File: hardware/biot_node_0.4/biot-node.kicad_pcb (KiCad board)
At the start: 2 copper layers, 13 parts, among them P1 ATSAMR21B, P2 ATSAMR21B-TEST-POINTs, P3 ATMEL-CORTEX, P4 FTDI/Serial, P5 On/Off Header, SW1 RESET, U1 MPU9250-Breakout

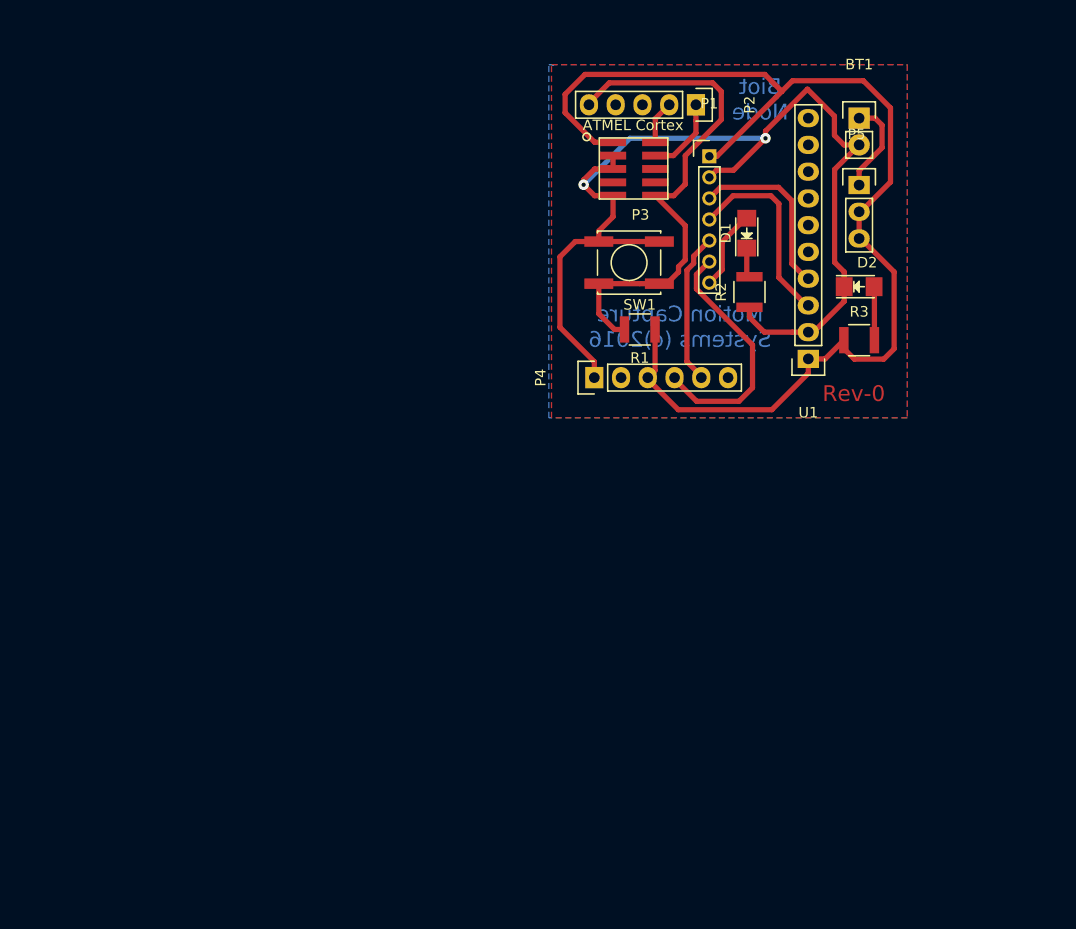
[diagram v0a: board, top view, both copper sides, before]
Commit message: Moving interface to newer Angular2 environment.
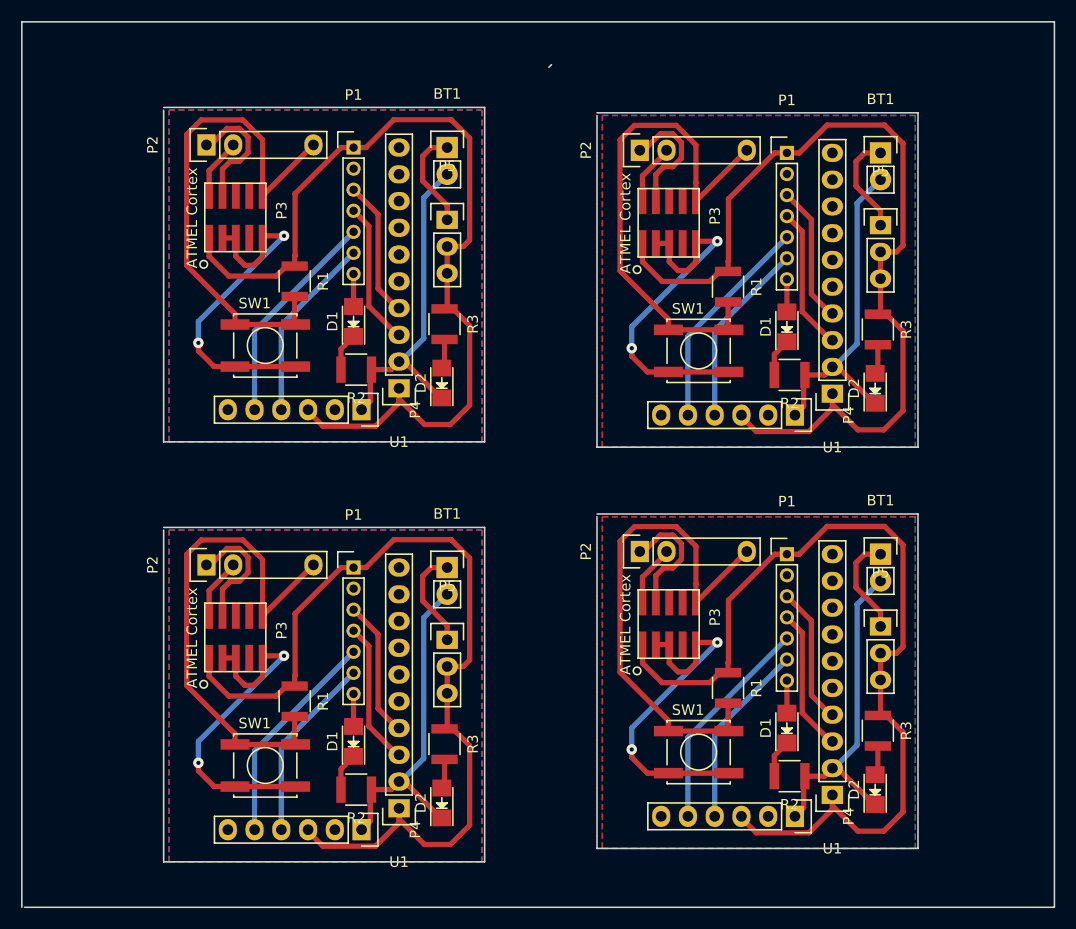
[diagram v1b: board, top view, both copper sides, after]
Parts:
- removed the BT1 at (168.7, 104.9)
- removed the D1 at (158.0, 115.8)
- removed the D2 at (168.7, 120.9)
- removed the P1 at (154.4, 108.5)
- removed the P2 at (153.2, 103.6)
- removed the P3 at (143.9, 112.7)
- removed the P4 at (143.5, 129.5)
- removed the P5 at (168.7, 111.3)
- removed the R1 at (147.8, 125.0)
- removed the R2 at (158.2, 121.4)
- removed the R3 at (168.7, 126.0)
- removed the SW1 at (146.8, 118.6)
- removed the U1 at (163.8, 127.8)
- added BT1: 1.5V, Pin_Headers:Pin_Header_Straight_1x02, F.Cu at (170.7, 146.3)
- added BT1: 1.5V, Pin_Headers:Pin_Header_Straight_1x02, F.Cu at (129.5, 147.6)
- added BT1: 1.5V, Pin_Headers:Pin_Header_Straight_1x02, F.Cu at (129.5, 107.7)
- added BT1: 1.5V, Pin_Headers:Pin_Header_Straight_1x02, F.Cu at (170.7, 108.2)
- added D1: SIGNAL, LEDs:LED_1206, F.Cu at (161.8, 162.8)
- added D1: SIGNAL, LEDs:LED_1206, F.Cu at (120.7, 164.1)
- added D1: SIGNAL, LEDs:LED_1206, F.Cu at (120.7, 124.2)
- added D1: SIGNAL, LEDs:LED_1206, F.Cu at (161.8, 124.7)
- added D2: PWR, LEDs:LED_1206, F.Cu at (170.2, 168.7)
- added D2: PWR, LEDs:LED_1206, F.Cu at (129.0, 169.9)
- added D2: PWR, LEDs:LED_1206, F.Cu at (129.0, 130.0)
- added D2: PWR, LEDs:LED_1206, F.Cu at (170.2, 130.6)
- added P1: ATSAMR21B, Pin_Headers:Pin_Header_Straight_1x07_Pitch2.00mm, F.Cu at (161.8, 146.3)
- added P1: ATSAMR21B, Pin_Headers:Pin_Header_Straight_1x07_Pitch2.00mm, F.Cu at (120.7, 147.6)
- added P1: ATSAMR21B, Pin_Headers:Pin_Header_Straight_1x07_Pitch2.00mm, F.Cu at (120.7, 107.7)
- added P1: ATSAMR21B, Pin_Headers:Pin_Header_Straight_1x07_Pitch2.00mm, F.Cu at (161.8, 108.2)
- added P2: ATSAMR21B-TEST-POINTs, Pin_Headers:Pin_Header_Straight_1x05, F.Cu at (147.8, 146.1)
- added P2: ATSAMR21B-TEST-POINTs, Pin_Headers:Pin_Header_Straight_1x05, F.Cu at (106.7, 147.3)
- added P2: ATSAMR21B-TEST-POINTs, Pin_Headers:Pin_Header_Straight_1x05, F.Cu at (106.7, 107.4)
- added P2: ATSAMR21B-TEST-POINTs, Pin_Headers:Pin_Header_Straight_1x05, F.Cu at (147.8, 108.0)
- added P3: ATMEL-CORTEX, atmelSAM:ATMEL_cortex_header_smd, F.Cu at (153.6, 156.3)
- added P3: ATMEL-CORTEX, atmelSAM:ATMEL_cortex_header_smd, F.Cu at (112.4, 157.6)
- added P3: ATMEL-CORTEX, atmelSAM:ATMEL_cortex_header_smd, F.Cu at (112.4, 117.7)
- added P3: ATMEL-CORTEX, atmelSAM:ATMEL_cortex_header_smd, F.Cu at (153.6, 118.2)
- added P4: FTDI/Serial, Pin_Headers:Pin_Header_Straight_1x06, F.Cu at (162.6, 171.2)
- added P4: FTDI/Serial, Pin_Headers:Pin_Header_Straight_1x06, F.Cu at (121.4, 172.5)
- added P4: FTDI/Serial, Pin_Headers:Pin_Header_Straight_1x06, F.Cu at (121.4, 132.6)
- added P4: FTDI/Serial, Pin_Headers:Pin_Header_Straight_1x06, F.Cu at (162.6, 133.1)
- added P5: On/Off Header, Pin_Headers:Pin_Header_Straight_1x03, F.Cu at (170.7, 153.2)
- added P5: On/Off Header, Pin_Headers:Pin_Header_Straight_1x03, F.Cu at (129.5, 154.4)
- added P5: On/Off Header, Pin_Headers:Pin_Header_Straight_1x03, F.Cu at (129.5, 114.6)
- added P5: On/Off Header, Pin_Headers:Pin_Header_Straight_1x03, F.Cu at (170.7, 115.1)
- added R1: 10k, Resistors_SMD:R_1210, F.Cu at (156.2, 159.0)
- added R1: 10k, Resistors_SMD:R_1210, F.Cu at (115.1, 160.3)
- added R1: 10k, Resistors_SMD:R_1210, F.Cu at (115.1, 120.4)
- added R1: 10k, Resistors_SMD:R_1210, F.Cu at (156.2, 120.9)
- added R2: 39, Resistors_SMD:R_1210, F.Cu at (162.1, 167.4)
- added R2: 39, Resistors_SMD:R_1210, F.Cu at (120.9, 168.7)
- added R2: 39, Resistors_SMD:R_1210, F.Cu at (120.9, 128.8)
- added R2: 39, Resistors_SMD:R_1210, F.Cu at (162.1, 129.3)
- added R3: 39, Resistors_SMD:R_1210, F.Cu at (170.4, 163.1)
- added R3: 39, Resistors_SMD:R_1210, F.Cu at (129.3, 164.3)
- added R3: 39, Resistors_SMD:R_1210, F.Cu at (129.3, 124.5)
- added R3: 39, Resistors_SMD:R_1210, F.Cu at (170.4, 125.0)
- added SW1: RESET, Buttons_Switches_SMD:SW_SPST_EVPBF, F.Cu at (153.4, 165.1)
- added SW1: RESET, Buttons_Switches_SMD:SW_SPST_EVPBF, F.Cu at (112.3, 166.4)
- added SW1: RESET, Buttons_Switches_SMD:SW_SPST_EVPBF, F.Cu at (112.3, 126.5)
- added SW1: RESET, Buttons_Switches_SMD:SW_SPST_EVPBF, F.Cu at (153.4, 127.0)
- added U1: MPU9250-Breakout, Pin_Headers:Pin_Header_Straight_1x10, F.Cu at (166.1, 169.2)
- added U1: MPU9250-Breakout, Pin_Headers:Pin_Header_Straight_1x10, F.Cu at (125.0, 170.4)
- added U1: MPU9250-Breakout, Pin_Headers:Pin_Header_Straight_1x10, F.Cu at (125.0, 130.6)
- added U1: MPU9250-Breakout, Pin_Headers:Pin_Header_Straight_1x10, F.Cu at (166.1, 131.1)
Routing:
- net +3V3: track 111.1 -> 347.8 mm
- net GND: track 104.3 -> 266.6 mm, vias 2 -> 8
- net NRST: track 50.0 -> 196.3 mm
- net RX: track 14.5 -> 83.1 mm
- net TX: track 23.6 -> 70.9 mm
- net SWDCLK: track 7.44 -> 48.1 mm
- net SCLK: track 18.8 -> 54.6 mm
- net SDA: track 16.9 -> 52.5 mm
- net Net-(BT1-Pad1): track 9.04 -> 38.7 mm
- net SWDIO: track 4.10 -> 23.1 mm
- net Net-(D1-Pad1): track 2.82 -> 14.6 mm
- net Net-(D2-Pad2): track 5.09 -> 11.3 mm
- net Net-(D1-Pad2): track 7.65 -> 12.4 mm
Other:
- board outline added: 98 x 84.1 mm
- board text removed: "Biot Node"
- board text removed: "Motion Capture Systems (c)2016"
- board text removed: "Rev-0"
